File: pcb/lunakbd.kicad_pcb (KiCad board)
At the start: 2 copper layers, 56 parts, among them SW1 Switch, SW10 Switch, SW11 Switch, SW12 Switch, SW13 Switch, SW14 Switch, SW15 Switch, SW16 Switch, SW17 Switch, SW18 Switch, SW19 Switch, SW2 Switch, SW20 Switch, SW21 Switch, SW22 Switch, SW23 Switch, SW24 Switch, SW25 Switch, SW26 Switch, SW27 Switch, SW28 Switch, SW3 Switch, SW4 Switch, SW5 Switch, SW6 Switch, SW7 Switch, SW8 Switch, SW9 Switch

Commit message: feat: pcb layout adjustments
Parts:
- SW28: footprint PCM_Switch_Keyboard_Cherry_MX:SW_Cherry_MX_PCB_1.00u -> PCM_Switch_Keyboard_Cherry_MX:SW_Cherry_MX_PCB_1.25u_90deg
- moved D28 9.21 mm to (149.3, 131.1), turned to 66.12 degrees
- moved SW25 2.77 mm to (84.0, 121.2), turned to 11.94 degrees
- moved D25 2.27 mm to (89.9, 124.2), turned to -78.06 degrees
- moved SW28 0.09 mm to (146.4, 125.5), turned to -23.88 degrees
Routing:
- net row-0: track 100.2 -> 0.00 mm
- net row-2: track 100.2 -> 0.00 mm
- net row-1: track 100.2 -> 0.00 mm
- net row-3: track 100.2 -> 0.00 mm
- net col-2: track 94.6 -> 0.00 mm
- net col-5: track 57.2 -> 0.00 mm
- net col-4: track 57.2 -> 0.00 mm
- net col-1: track 57.2 -> 0.00 mm
- net col-3: track 57.1 -> 0.00 mm
- net col-0: track 57.1 -> 0.00 mm
- net row-4: track 19.0 -> 0.00 mm

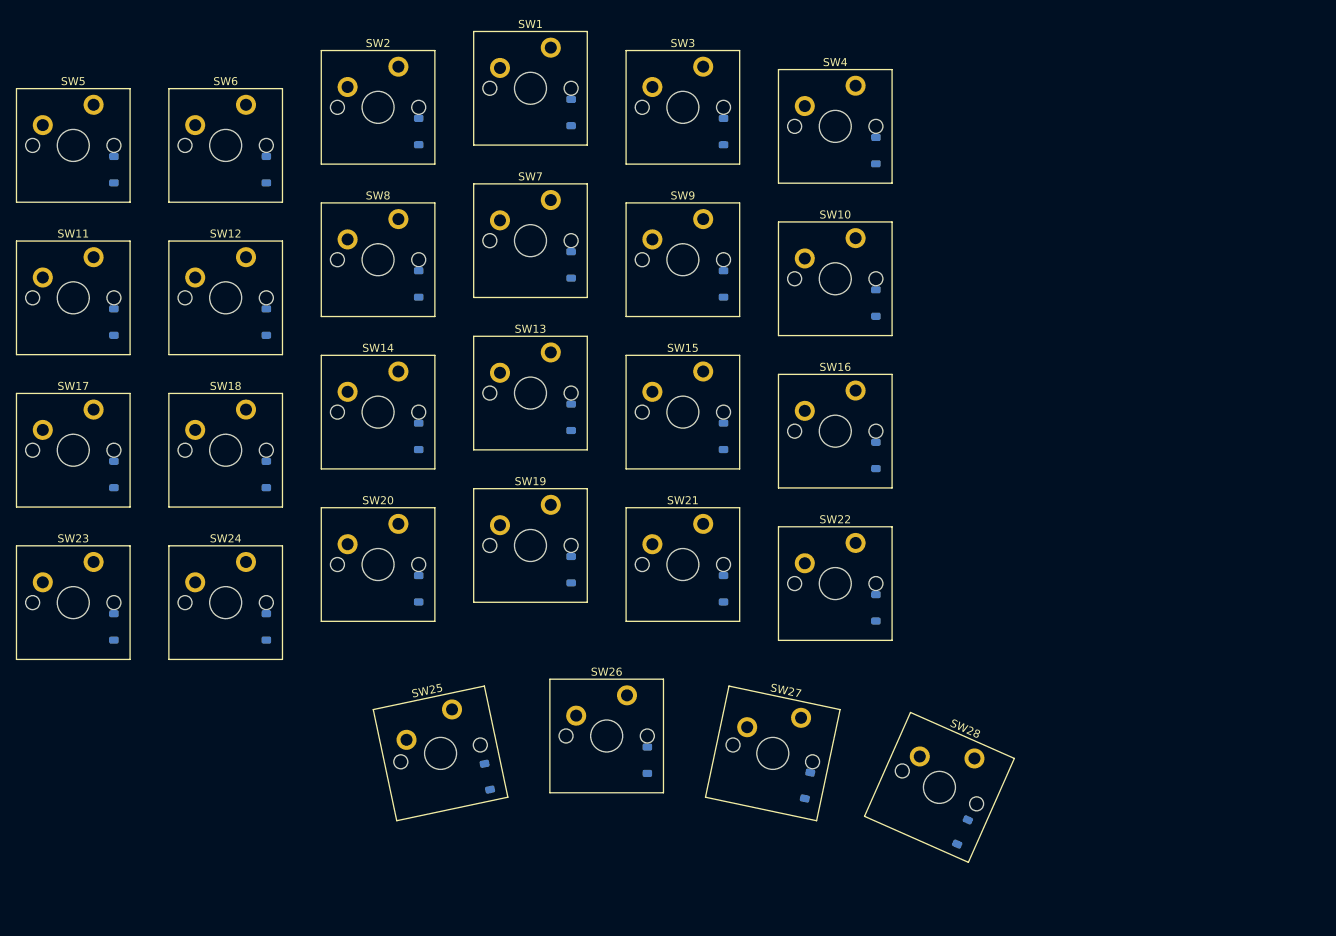
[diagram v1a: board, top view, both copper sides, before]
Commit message: fix: update switch numberation in pcb editor
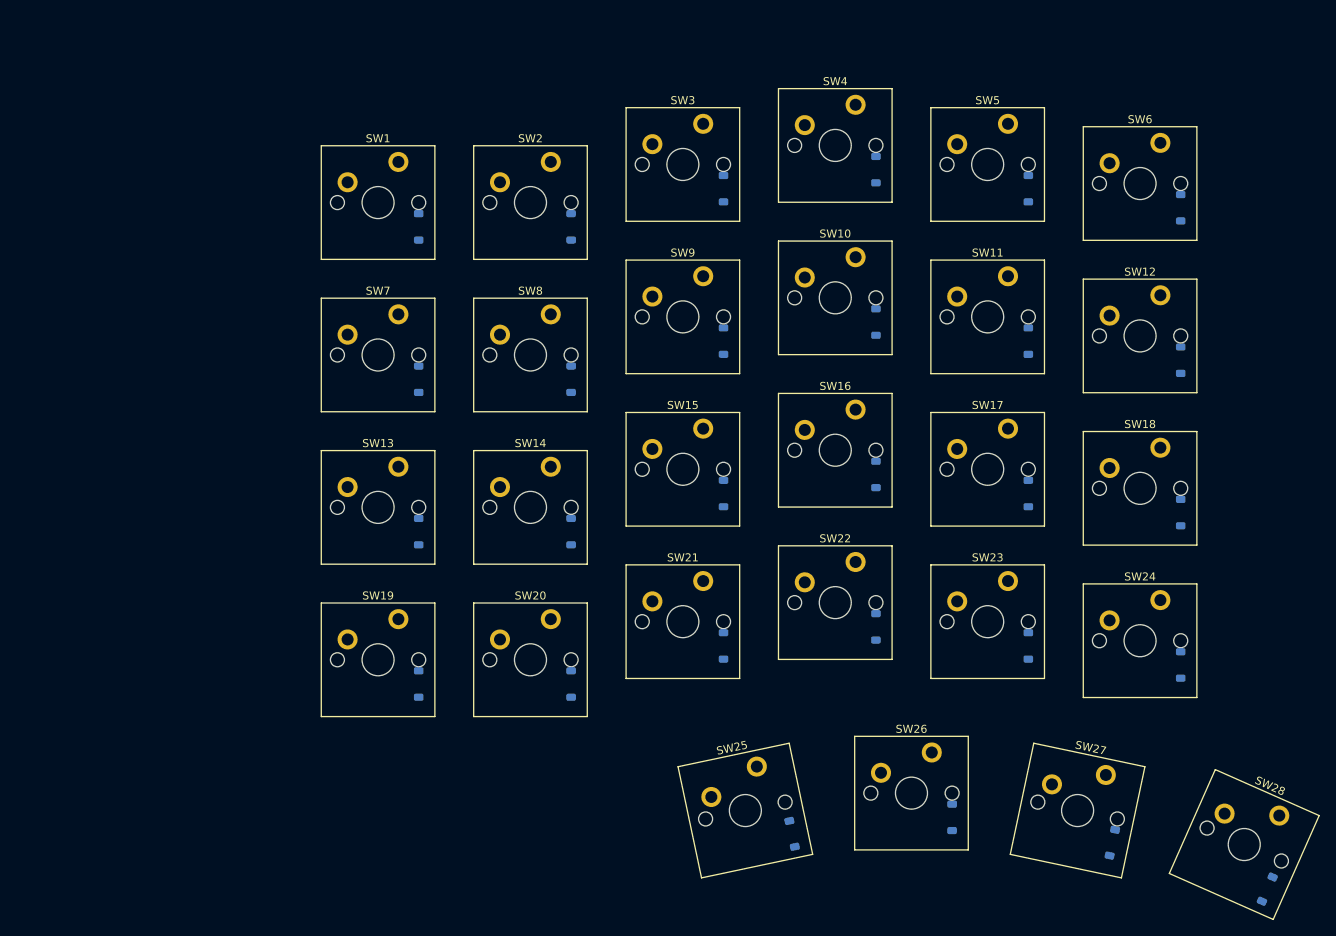
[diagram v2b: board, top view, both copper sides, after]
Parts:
- moved D10 38.8 mm to (138.4, 67.3)
- moved D16 38.8 mm to (138.4, 86.4)
- moved D22 38.8 mm to (138.4, 105.4)
- moved D26 38.8 mm to (148.0, 129.2)
- moved D4 38.8 mm to (138.4, 48.3)
- moved SW11 38.8 mm to (152.4, 66.7)
- moved SW17 38.8 mm to (152.4, 85.7)
- moved SW23 38.8 mm to (152.4, 104.8)
- moved SW25 38.8 mm to (122.1, 128.4)
- moved SW5 38.8 mm to (152.4, 47.6)
- moved D1 38.8 mm to (81.3, 55.4)
- moved D12 38.8 mm to (176.5, 72.1)
- moved D13 38.8 mm to (81.3, 93.5)
- moved D14 38.8 mm to (100.3, 93.5)
- moved D19 38.8 mm to (81.3, 112.6)
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- renumbered D5 to D1, D7 to D10, D9 to D11, D10 to D12, D17 to D13, D18 to D14, D14 to D15, D13 to D16, D15 to D17, D16 to D18, D23 to D19, D6 to D2, D24 to D20, D20 to D21, D19 to D22, D21 to D23, D22 to D24, D2 to D3, D1 to D4, D3 to D5, D4 to D6, D11 to D7, D12 to D8, D8 to D9, SW5 to SW1, SW7 to SW10, SW9 to SW11, SW10 to SW12, SW17 to SW13, SW18 to SW14, SW14 to SW15, SW13 to SW16, SW15 to SW17, SW16 to SW18, SW23 to SW19, SW6 to SW2, SW24 to SW20, SW20 to SW21, SW19 to SW22, SW21 to SW23, SW22 to SW24, SW2 to SW3, SW1 to SW4, SW3 to SW5, SW4 to SW6, SW11 to SW7, SW12 to SW8, SW8 to SW9
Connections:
- SW1 pad 1: col-4 -> col-0
- SW10 pad 1: col-0 -> col-3
- SW11 pad 1: col-2 -> col-4
- SW12 pad 1: col-3 -> col-5
- SW13 pad 1: col-4 -> col-0
- SW14 pad 1: col-5 -> col-1
- SW15 pad 1: col-1 -> col-2
- SW16 pad 1: col-0 -> col-3
- SW17 pad 1: col-2 -> col-4
- SW18 pad 1: col-3 -> col-5
- SW19 pad 1: col-4 -> col-0
- SW2 pad 1: col-5 -> col-1
- SW20 pad 1: col-5 -> col-1
- SW21 pad 1: col-1 -> col-2
- SW22 pad 1: col-0 -> col-3
- SW23 pad 1: col-2 -> col-4
- SW24 pad 1: col-3 -> col-5
- SW3 pad 1: col-1 -> col-2
- SW4 pad 1: col-0 -> col-3
- SW5 pad 1: col-2 -> col-4
- SW6 pad 1: col-3 -> col-5
- SW7 pad 1: col-4 -> col-0
- SW8 pad 1: col-5 -> col-1
- SW9 pad 1: col-1 -> col-2

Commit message: feat: complete schematic design
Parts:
- added D29: Diode, Diode_SMD:D_SOD-123, F.Cu at (223.8, 85.8)
- added J1: TRRS-PJ-320A, Connector_Audio:Jack_3.5mm_PJ320E_Horizontal, F.Cu at (259.2, 64.2)
- added J2: Battery_Socket, Connector_JST:JST_PH_S2B-PH-K_1x02_P2.00mm_Horizontal, F.Cu at (253.7, 85.3)
- added J3: Conn_Display, kbd:OLED, F.Cu at (245.6, 57.4)
- added SW29: Reset_Button, Keebio-Parts:SW_Tactile_SPST_Angled_MJTP1117-no-mount, F.Cu at (242.9, 87.4)
- added SW30: Battery_Switch, PCM_marbastlib-various:SW_MSK12C02-HB, F.Cu at (216.1, 87.5)
- added SW31: RotaryEncoder_SW, Rotary_Encoder:RotaryEncoder_Alps_EC11E-Switch_Vertical_H20mm, F.Cu at (224.1, 98.0)
- added U1: ProMicro, PCM_marbastlib-xp-promicroish:SuperMini_nRF52840_H_USBup, F.Cu at (225.7, 63.3)

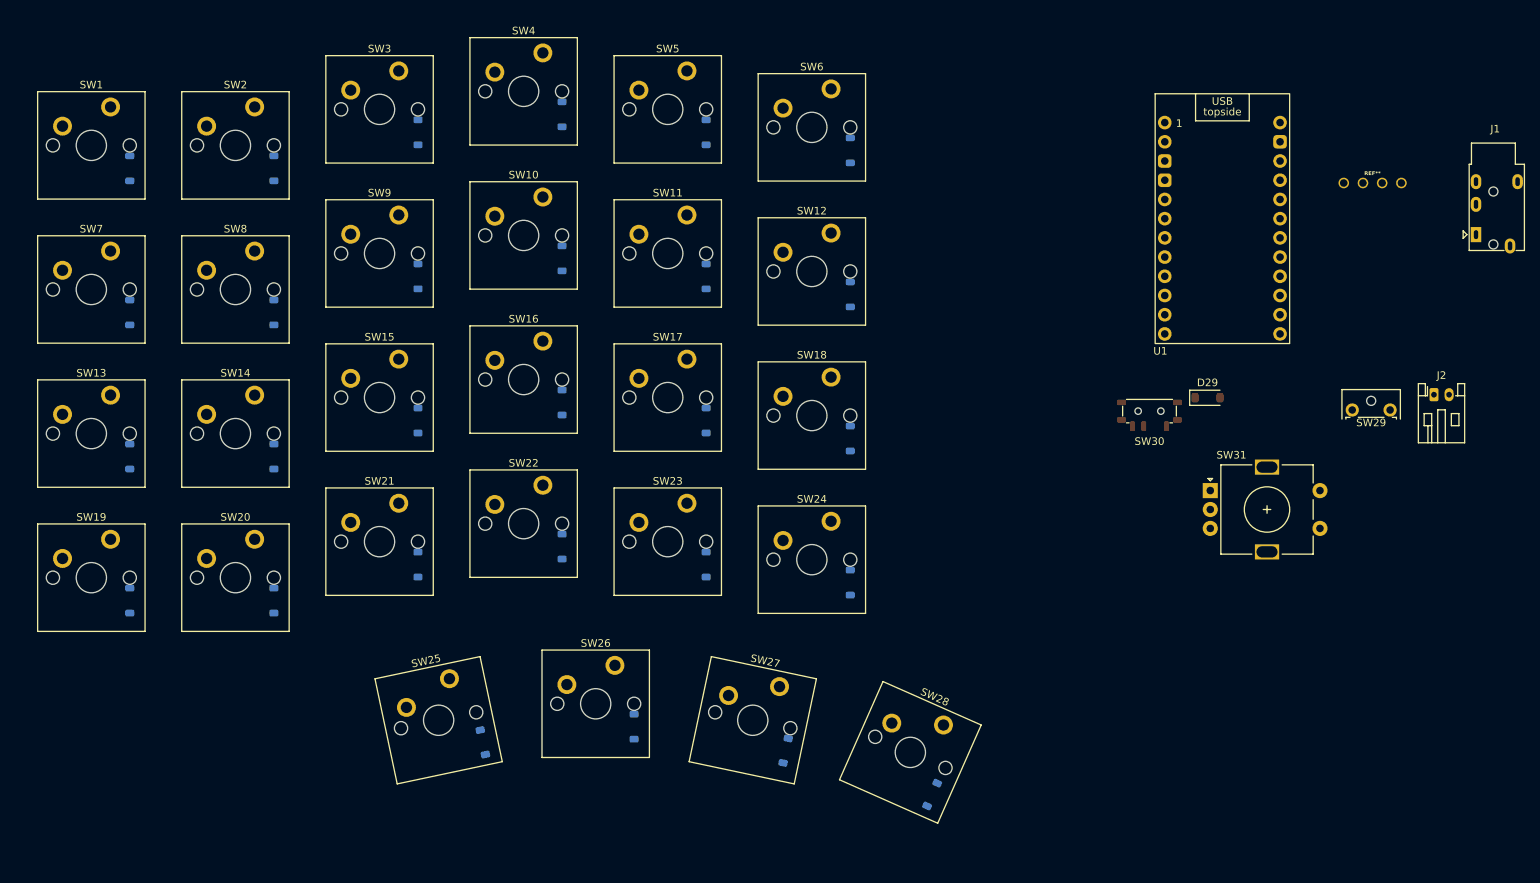
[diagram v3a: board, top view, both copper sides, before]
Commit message: feat: create edge cuts for pcb
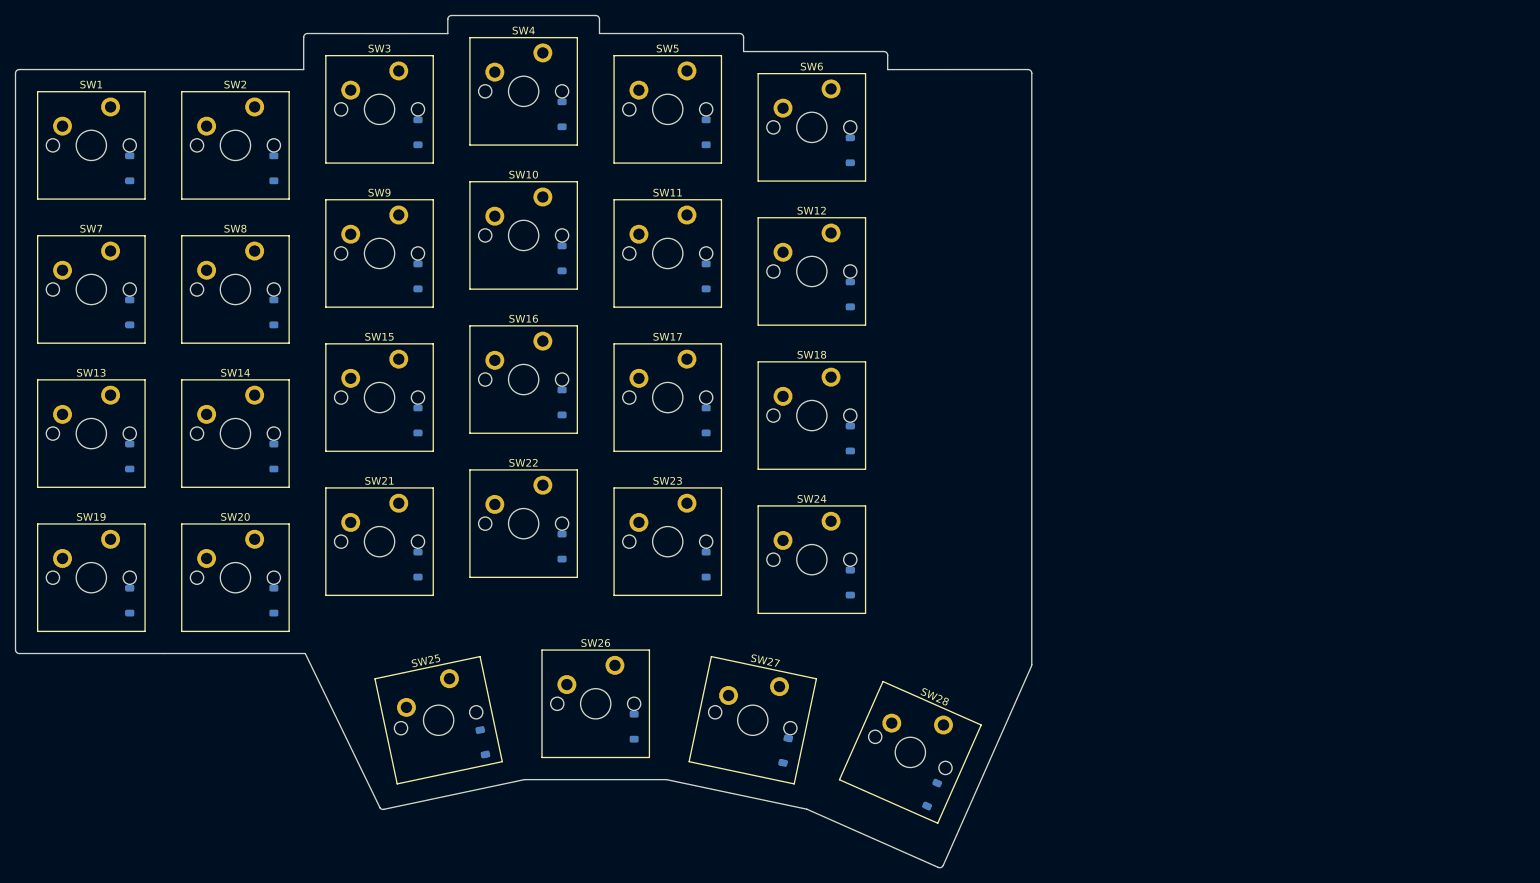
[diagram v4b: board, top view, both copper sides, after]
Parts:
- removed D29: Diode, Diode_SMD:D_SOD-123
- removed J1: TRRS-PJ-320A, Connector_Audio:Jack_3.5mm_PJ320E_Horizontal
- removed J2: Battery_Socket, Connector_JST:JST_PH_S2B-PH-K_1x02_P2.00mm_Horizontal
- removed J3: Conn_Display, kbd:OLED
- removed SW29: Reset_Button, Keebio-Parts:SW_Tactile_SPST_Angled_MJTP1117-no-mount
- removed SW30: Battery_Switch, PCM_marbastlib-various:SW_MSK12C02-HB
- removed SW31: RotaryEncoder_SW, Rotary_Encoder:RotaryEncoder_Alps_EC11E-Switch_Vertical_H20mm
- removed U1: ProMicro, PCM_marbastlib-xp-promicroish:SuperMini_nRF52840_H_USBup
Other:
- board outline added: 134.4 x 112.7 mm

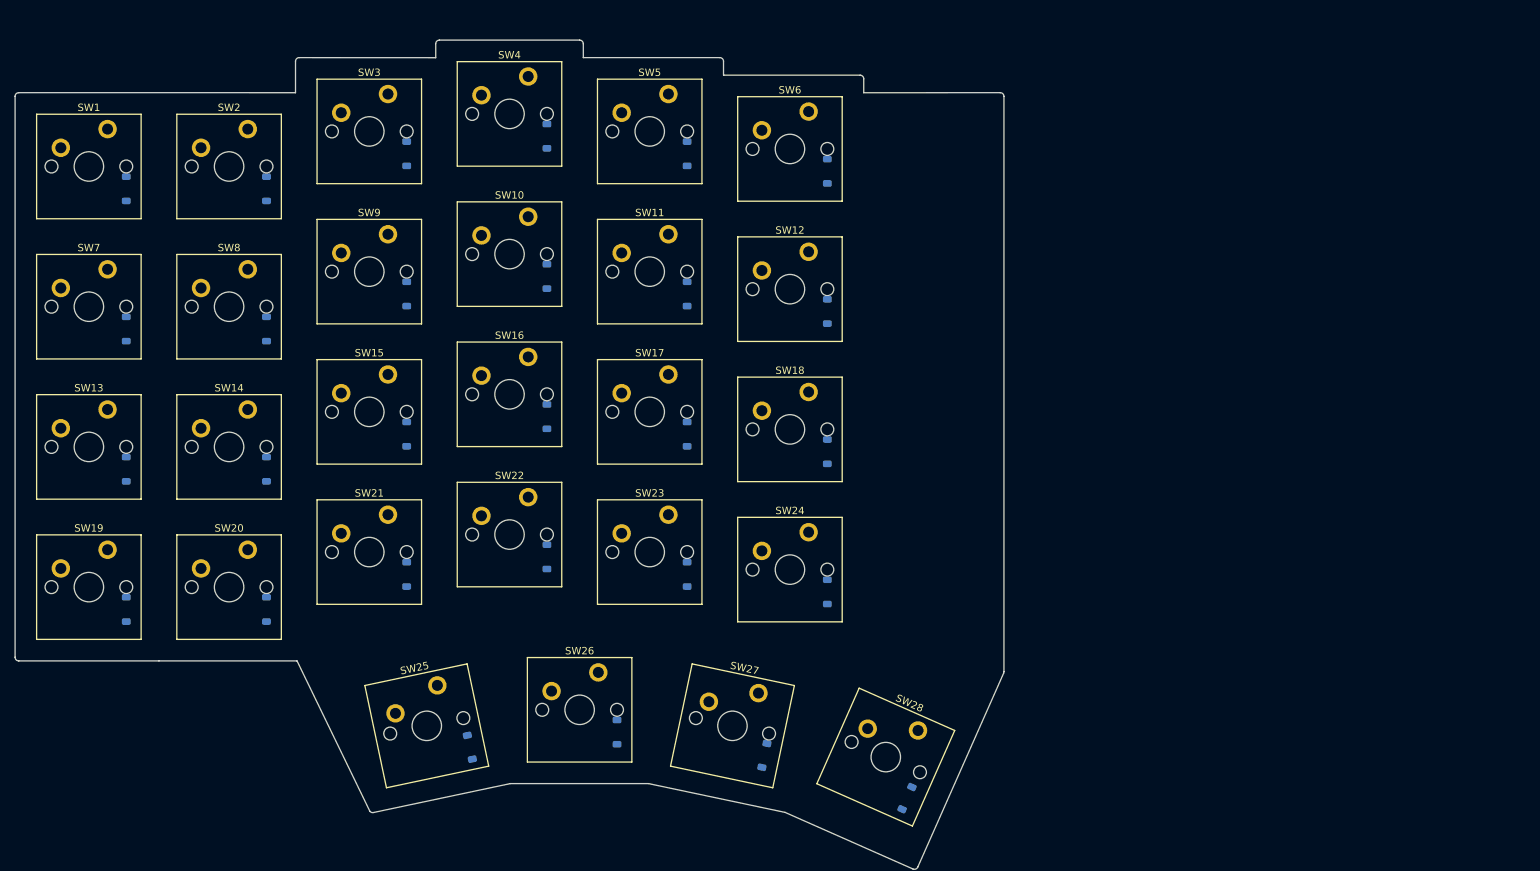
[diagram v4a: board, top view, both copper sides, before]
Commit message: feat: update footprints and place promicro and oled display
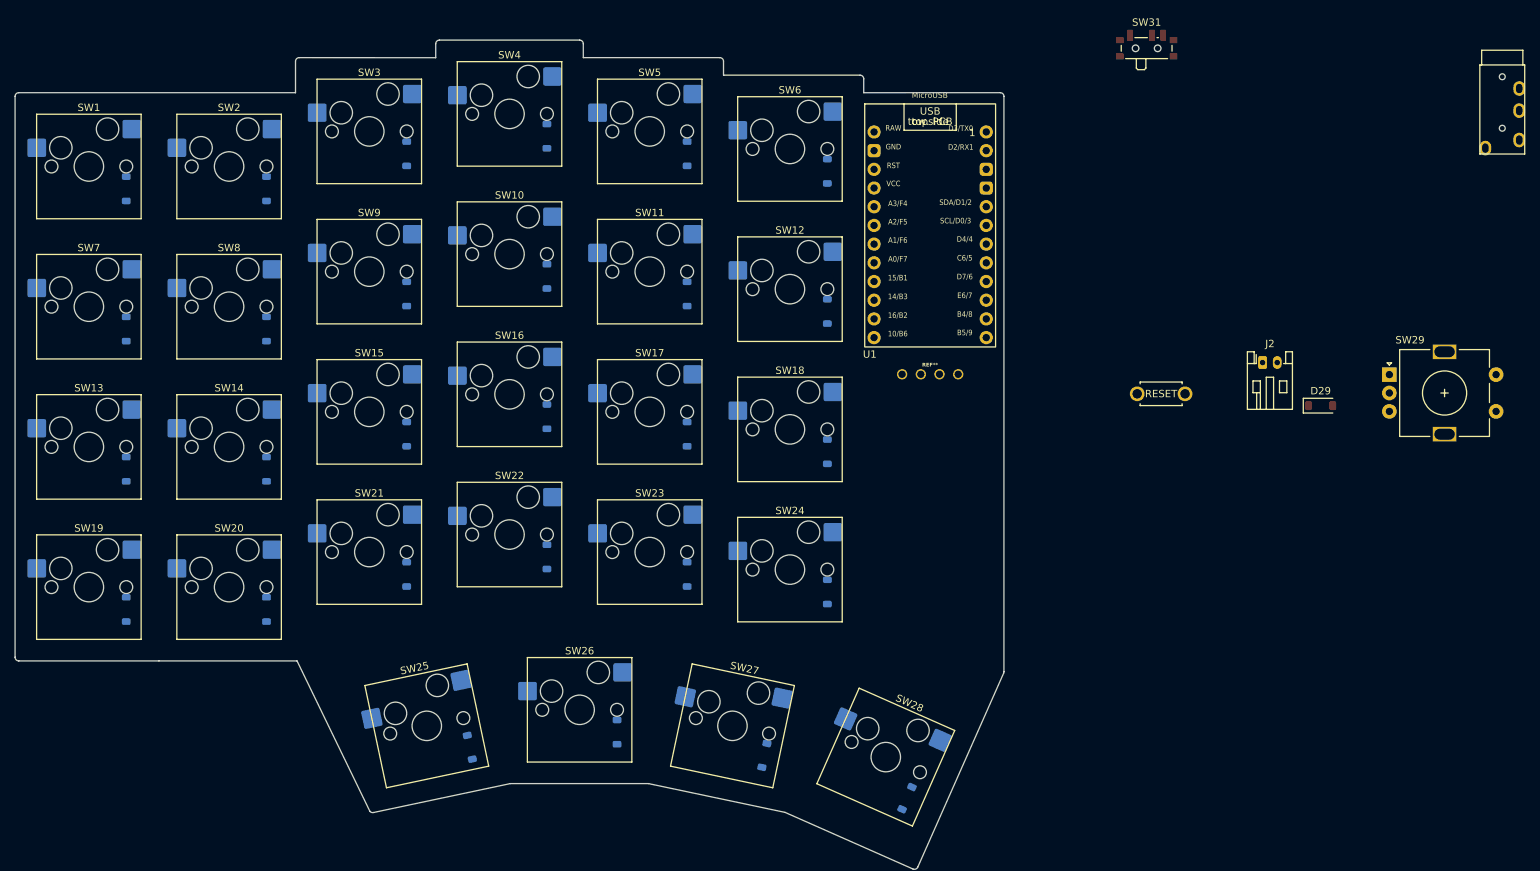
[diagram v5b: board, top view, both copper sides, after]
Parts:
- added D29: Diode, Diode_SMD:D_SOD-123, F.Cu at (243.6, 84.9)
- added J1: TRRS-PJ-320A, Keebio-Parts:TRRS-PJ-320A-no-Fmask, F.Cu at (268.2, 38.6)
- added J2: Battery_Socket, Connector_JST:JST_PH_S2B-PH-K_1x02_P2.00mm_Horizontal, F.Cu at (235.7, 79.0)
- added J3: Conn_Display, kbd:OLED, F.Cu at (190.5, 80.6)
- added SW29: RotaryEncoder_SW, Rotary_Encoder:RotaryEncoder_Alps_EC11E-Switch_Vertical_H20mm, F.Cu at (252.9, 80.7)
- added SW30: Reset_Button, kbd:ResetSW, F.Cu at (221.9, 83.3)
- added SW31: Battery_Switch, Button_Switch_SMD:SW_SPDT_PCM12, F.Cu at (219.9, 36.0)
- added U1: SuperMini_nRF52840_H_USBdn, PCM_marbastlib-xp-promicroish:SuperMini_nRF52840_H_USBdn, F.Cu at (190.5, 61.7)
- SW1, SW10, SW11, SW12, SW13, SW14, SW15, SW16, SW17, SW18, SW19, SW2, SW20, SW21, SW22, SW23, SW24, SW25, SW26, SW27, SW3, SW4, SW5, SW6, SW7, SW8, SW9: footprint PCM_Switch_Keyboard_Cherry_MX:SW_Cherry_MX_PCB_1.00u -> PCM_Switch_Keyboard_Hotswap_Kailh:SW_Hotswap_Kailh_MX_1.00u
- SW28: footprint PCM_Switch_Keyboard_Cherry_MX:SW_Cherry_MX_PCB_1.25u_90deg -> PCM_Switch_Keyboard_Hotswap_Kailh:SW_Hotswap_Kailh_MX_1.25u_90deg
- turned SW28 to -23.879 degrees
